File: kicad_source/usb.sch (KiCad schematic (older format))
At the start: 18 parts, among them CN4 10118192-0001LF, Q2 BC847, U4 FT230XS

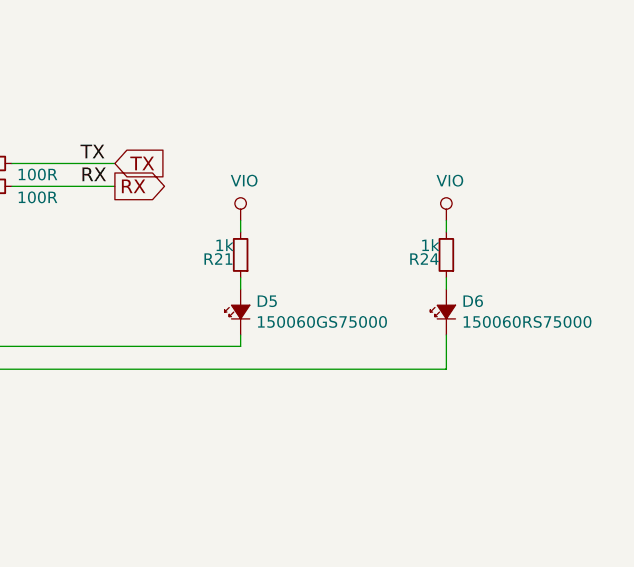
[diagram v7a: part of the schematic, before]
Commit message: connected interrupt line of BMA253, updated layout
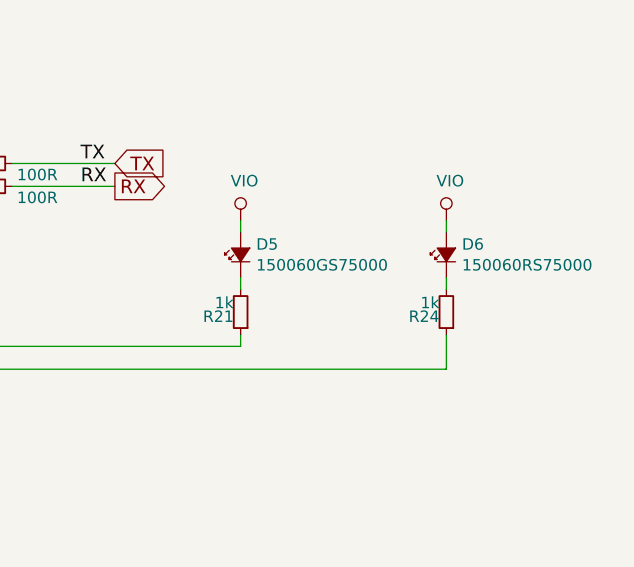
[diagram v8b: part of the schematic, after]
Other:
- moved on the sheet: D5, D6, R21, R24
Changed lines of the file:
@@
 L devices:Led_Small D?
 U 1 1 5CB4794B
-P 8200 3000
+P 8200 2750
 AR Path="/5CB4794B" Ref="D?"  Part="1"
 AR Path="/5CB34EF4/5CB4794B" Ref="D?"  Part="1"
 AR Path="/5EB35E34/5CB4794B" Ref="D5"  Part="1"
-F 0 "D5" V 8246 2932 50  0000 R CNN
-F 1 "150060GS75000" V 8155 2932 50  0000 R CNN
-F 2 "LEDs:LED_0603" V 8200 3000 50  0001 C CNN
-F 3 "" V 8200 3000 50  0000 C CNN
-	1    8200 3000
+F 0 "D5" V 8246 2682 50  0000 R CNN
+F 1 "150060GS75000" V 8155 2682 50  0000 R CNN
+F 2 "LEDs:LED_0603" V 8200 2750 50  0001 C CNN
+F 3 "" V 8200 2750 50  0000 C CNN
+	1    8200 2750
 	0    -1   -1   0
 $EndComp
@@
 L devices:Led_Small D?
 U 1 1 5CB47952
-P 9100 3000
+P 9100 2750
 AR Path="/5CB47952" Ref="D?"  Part="1"
 AR Path="/5CB34EF4/5CB47952" Ref="D?"  Part="1"
 AR Path="/5EB35E34/5CB47952" Ref="D6"  Part="1"
-F 0 "D6" V 9146 2932 50  0000 R CNN
-F 1 "150060RS75000" V 9055 2932 50  0000 R CNN
-F 2 "LEDs:LED_0603" V 9100 3000 50  0001 C CNN
-F 3 "" V 9100 3000 50  0000 C CNN
-	1    9100 3000
+F 0 "D6" V 9146 2682 50  0000 R CNN
+F 1 "150060RS75000" V 9055 2682 50  0000 R CNN
+F 2 "LEDs:LED_0603" V 9100 2750 50  0001 C CNN
+F 3 "" V 9100 2750 50  0000 C CNN
+	1    9100 2750
 	0    -1   -1   0
 $EndComp
@@
 L devices:R_1206 R?
 U 1 1 5CB47959
-P 8200 2750
+P 8200 3000
 AR Path="/5CB47959" Ref="R?"  Part="1"
 AR Path="/5CB34EF4/5CB47959" Ref="R?"  Part="1"
 AR Path="/5EB35E34/5CB47959" Ref="R21"  Part="1"
-F 0 "R21" H 8230 2770 50  0000 L CNN
-F 1 "1k" H 8230 2710 50  0000 L CNN
-F 2 "resistors:R_0603" H 8200 2600 50  0001 C CNN
-F 3 "" H 8200 2750 50  0000 C CNN
-	1    8200 2750
+F 0 "R21" H 8230 3020 50  0000 L CNN
+F 1 "1k" H 8230 2960 50  0000 L CNN
+F 2 "resistors:R_0603" H 8200 2850 50  0001 C CNN
+F 3 "" H 8200 3000 50  0000 C CNN
+	1    8200 3000
 	-1   0    0    1
 $EndComp
@@
 L devices:R_1206 R?
 U 1 1 5CB47960
-P 9100 2750
+P 9100 3000
 AR Path="/5CB47960" Ref="R?"  Part="1"
 AR Path="/5CB34EF4/5CB47960" Ref="R?"  Part="1"
 AR Path="/5EB35E34/5CB47960" Ref="R24"  Part="1"
-F 0 "R24" H 9130 2770 50  0000 L CNN
-F 1 "1k" H 9130 2710 50  0000 L CNN
-F 2 "resistors:R_0603" H 9100 2600 50  0001 C CNN
-F 3 "" H 9100 2750 50  0000 C CNN
-	1    9100 2750
+F 0 "R24" H 9130 3020 50  0000 L CNN
+F 1 "1k" H 9130 2960 50  0000 L CNN
+F 2 "resistors:R_0603" H 9100 2850 50  0001 C CNN
+F 3 "" H 9100 3000 50  0000 C CNN
+	1    9100 3000
 	-1   0    0    1
 $EndComp
@@
 	9100 2600 9100 2650
 Wire Wire Line
-	8200 2850 8200 2900
-Wire Wire Line
-	9100 2850 9100 2900
-Wire Wire Line
 	8200 3100 8200 3150
 Wire Wire Line
@@
 Wire Wire Line
 	6450 3250 9100 3250
+Wire Wire Line
+	9100 2850 9100 2900
+Wire Wire Line
+	8200 2850 8200 2900
 $EndSCHEMATC
